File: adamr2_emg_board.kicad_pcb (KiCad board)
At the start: 2 copper layers, 50 x 50 mm, 7 parts, among them J1 Screw_Terminal_01x02, J2 Conn_01x02, J3 Screw_Terminal_01x02, K1 G6C-1114P-US

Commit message: Update
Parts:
- removed the REF** at (86.0, 94.0)
- removed the REF** at (126.0, 94.0)
- added REF**: MountingHole_3.2mm_M3, MountingHole:MountingHole_3.2mm_M3, F.Cu at (175.0, 69.8)
- added REF**: MountingHole_3.2mm_M3, MountingHole:MountingHole_3.2mm_M3, F.Cu at (124.5, 69.8)
- moved F1 52.8 mm to (171.0, 91.0)
- moved K1 51.1 mm to (154.0, 99.0), turned to 180 degrees
- moved J3 48.0 mm to (132.0, 99.0)
- moved J1 46.3 mm to (132.0, 84.0)
- moved J2 44.8 mm to (149.0, 85.0), turned to 90 degrees
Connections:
- K1 pad 3: Net-(F1-Pad2) -> Net-(J3-Pad2)
- K1 pad 4: Net-(J3-Pad2) -> Net-(F1-Pad2)
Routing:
- net VCC: track 60.0 -> 0.00 mm
- net Net-(F1-Pad2): track 28.1 -> 0.00 mm
- net Net-(J3-Pad2): track 14.8 -> 0.06 mm
- net Net-(J2-Pad1): track 9.98 -> 0.32 mm
- net GND: track 33.6 -> 28.0 mm
- removed copper zone on B.Cu, net GND
- removed copper zone on F.Cu, net GND
- removed copper zone on F.Cu, net Net-(F1-Pad2)
- removed copper zone on F.Cu, net Net-(J3-Pad2)
- removed copper zone on F.Cu, net VCC
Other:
- board size 50 x 50 mm -> 60 x 45 mm
- board text removed: "+24V"
- board text removed: "Emergency Switch"
- board text removed: "GND"
- board text removed: "INPUT"
- board text removed: "OUTPUT"
- board text removed: "Φ5.2x20mm Glass Tube Fuse"

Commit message: Update
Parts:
- removed J3: Screw_Terminal_01x02, adamr2_footprints:OSTYK21102030
- J1: value Screw_Terminal_01x02 -> Screw_Terminal_01x04; footprint adamr2_footprints:OSTYK21102030 -> adamr2_footprints:OSTYK21104030
- moved J1 8.81 mm to (133.3, 92.7)
- moved J2 4.82 mm to (153.7, 83.8)
- moved K1 2.21 mm to (156.2, 99.0)
- moved F1 1.72 mm to (172.7, 91.0)
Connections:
- J1 pad 2: VCC -> Net-(J1-Pad2)
- K1 pad 3: Net-(J3-Pad2) -> Net-(J1-Pad2)
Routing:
- net VCC: track 0.00 -> 48.4 mm
- net Net-(J1-Pad2): track 0.00 -> 26.3 mm
- net Net-(F1-Pad2): track 0.00 -> 16.2 mm
- net Net-(J2-Pad1): track 0.32 -> 13.3 mm
- net GND: track 28.0 -> 37.7 mm
- added copper zone on B.Cu, net GND
- added copper zone on F.Cu, net GND
- added copper zone on F.Cu, net Net-(F1-Pad2)
- added copper zone on F.Cu, net Net-(J1-Pad2)
- added copper zone on F.Cu, net VCC
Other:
- board text added: "5.2x20mm Glass Tube Fuse"
- board text added: "G6C-1114P-US DC24V"
- board text added: "GND"
- board text added: "INPUT"
- board text added: "OUTPUT"
- board text added: "VCC"
- board text added: "XH Conn"

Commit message: Update
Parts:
- added REF**: MountingHole_3.2mm_M3, MountingHole:MountingHole_3.2mm_M3, F.Cu at (118.0, 105.0)
- added REF**: MountingHole_3.2mm_M3, MountingHole:MountingHole_3.2mm_M3, F.Cu at (180.0, 105.0)
- moved REF** 12.0 mm to (118.0, 80.0)
- moved REF** 11.3 mm to (180.0, 80.0)
- moved F1 1.71 mm to (172.7, 92.7)
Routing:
- net VCC: track 48.4 -> 47.0 mm
- net Net-(F1-Pad2): track 16.2 -> 16.9 mm
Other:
- board size 60 x 45 mm -> 70 x 33 mm

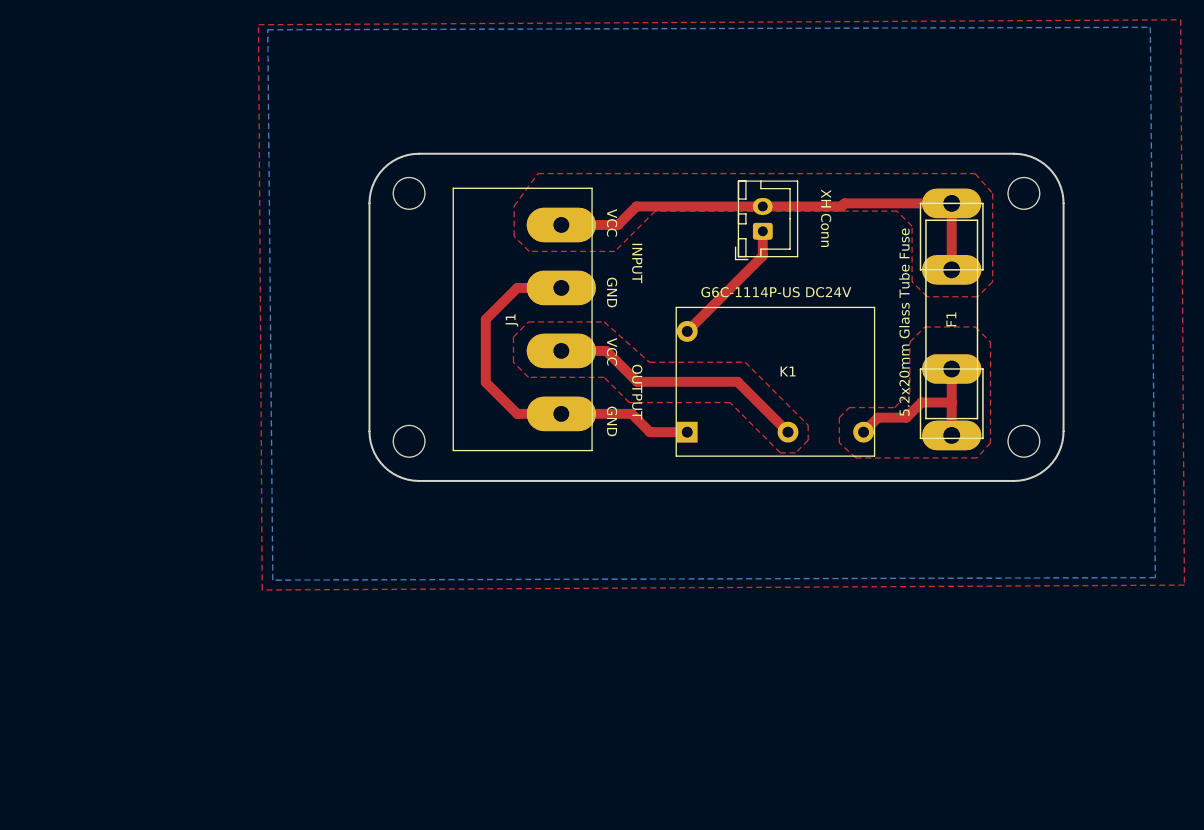
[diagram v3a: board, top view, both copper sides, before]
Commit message: Update: ヒューズホルダの種類を変更した
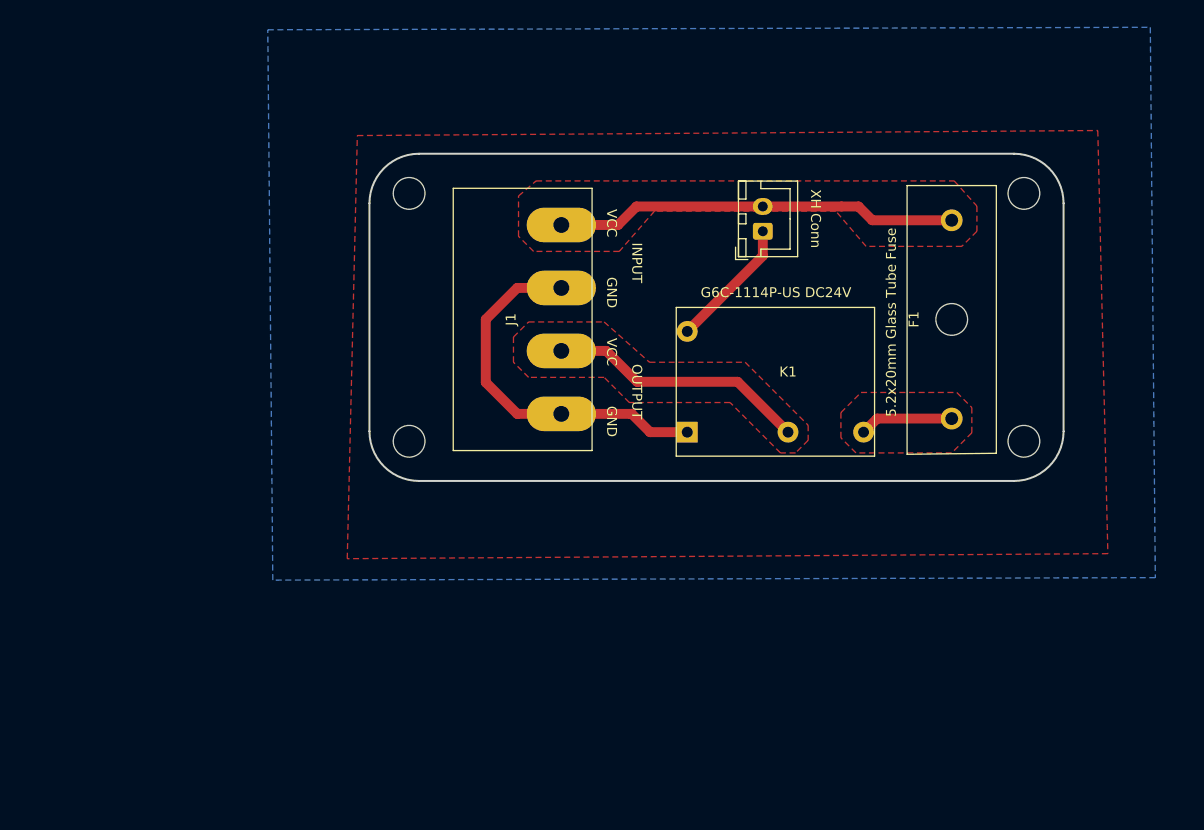
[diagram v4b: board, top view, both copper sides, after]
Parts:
- F1: footprint adamr2_footprints:FUC-03A -> adamr2_footprints:F-60-A
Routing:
- net Net-(F1-Pad2): track 16.9 -> 9.52 mm
- net VCC: track 47.0 -> 40.7 mm

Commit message: Update: 表面をVCC，裏面をGNDのベタにした
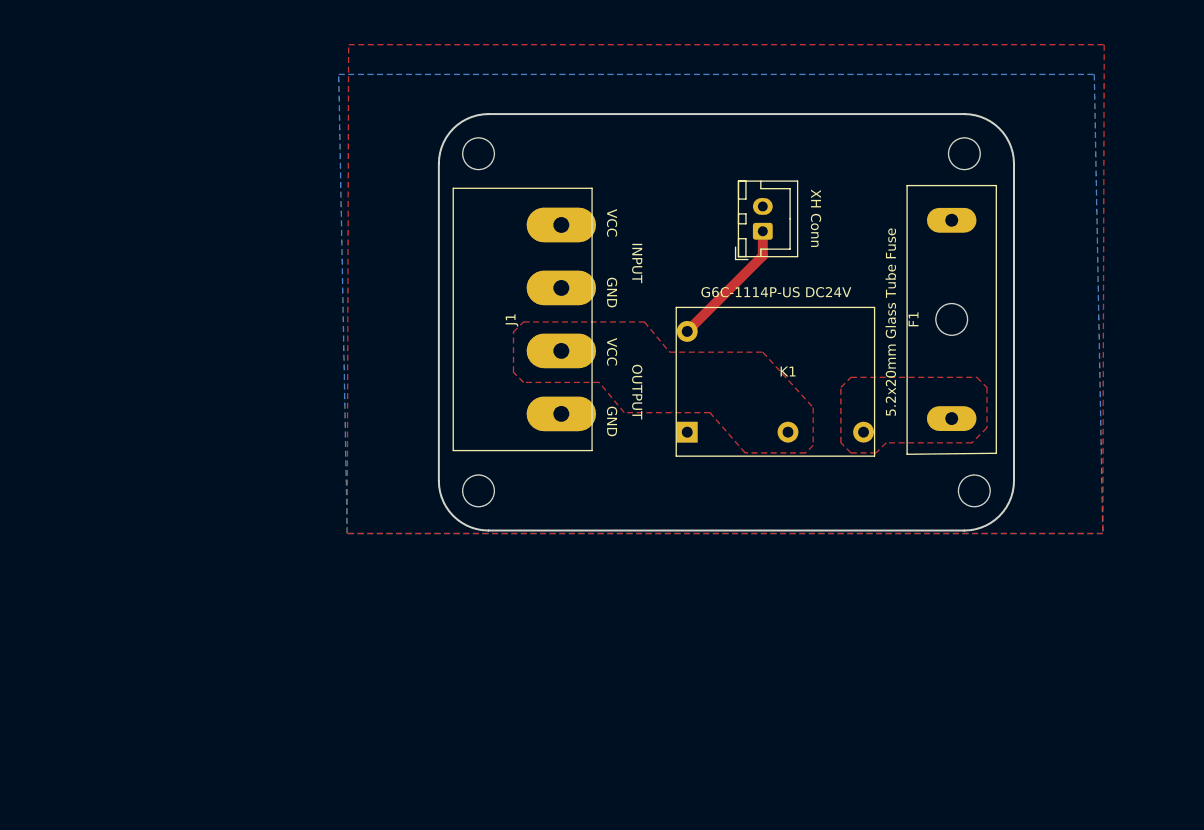
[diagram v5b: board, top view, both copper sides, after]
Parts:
- removed the REF** at (118.0, 80.0)
- removed the REF** at (118.0, 105.0)
- removed the REF** at (180.0, 105.0)
- removed the REF** at (180.0, 80.0)
- added REF**: MountingHole_3.2mm_M3, MountingHole:MountingHole_3.2mm_M3, F.Cu at (125.0, 76.0)
- added REF**: MountingHole_3.2mm_M3, MountingHole:MountingHole_3.2mm_M3, F.Cu at (125.0, 110.0)
- added REF**: MountingHole_3.2mm_M3, MountingHole:MountingHole_3.2mm_M3, F.Cu at (175.0, 110.0)
- added REF**: MountingHole_3.2mm_M3, MountingHole:MountingHole_3.2mm_M3, F.Cu at (174.0, 76.0)
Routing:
- net VCC: track 40.7 -> 0.00 mm
- net GND: track 37.7 -> 0.00 mm
- net Net-(J1-Pad2): track 26.3 -> 0.00 mm
- net Net-(F1-Pad2): track 9.52 -> 0.06 mm
- removed copper zone on F.Cu, net GND
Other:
- board size 70 x 33 mm -> 58 x 42 mm

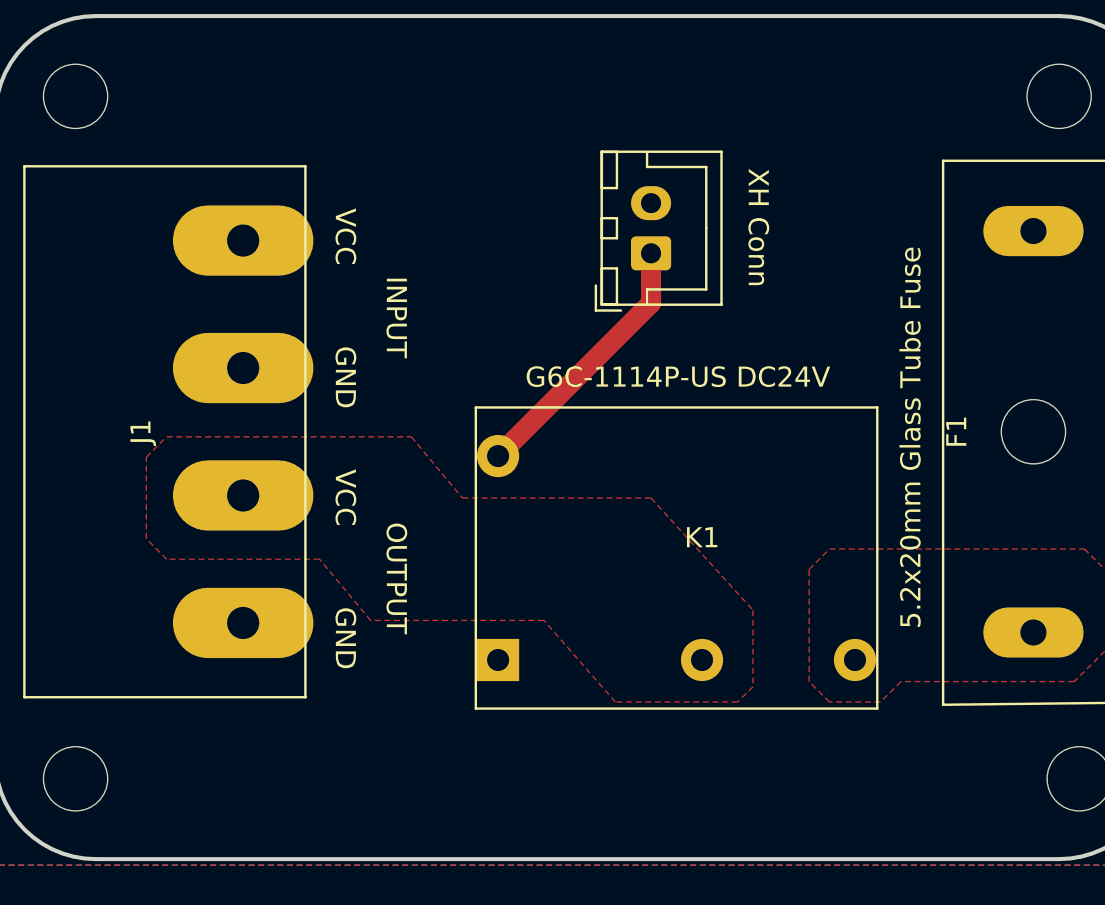
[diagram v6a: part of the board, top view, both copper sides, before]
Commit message: Update: シルクを少し調整，寸法線を追加
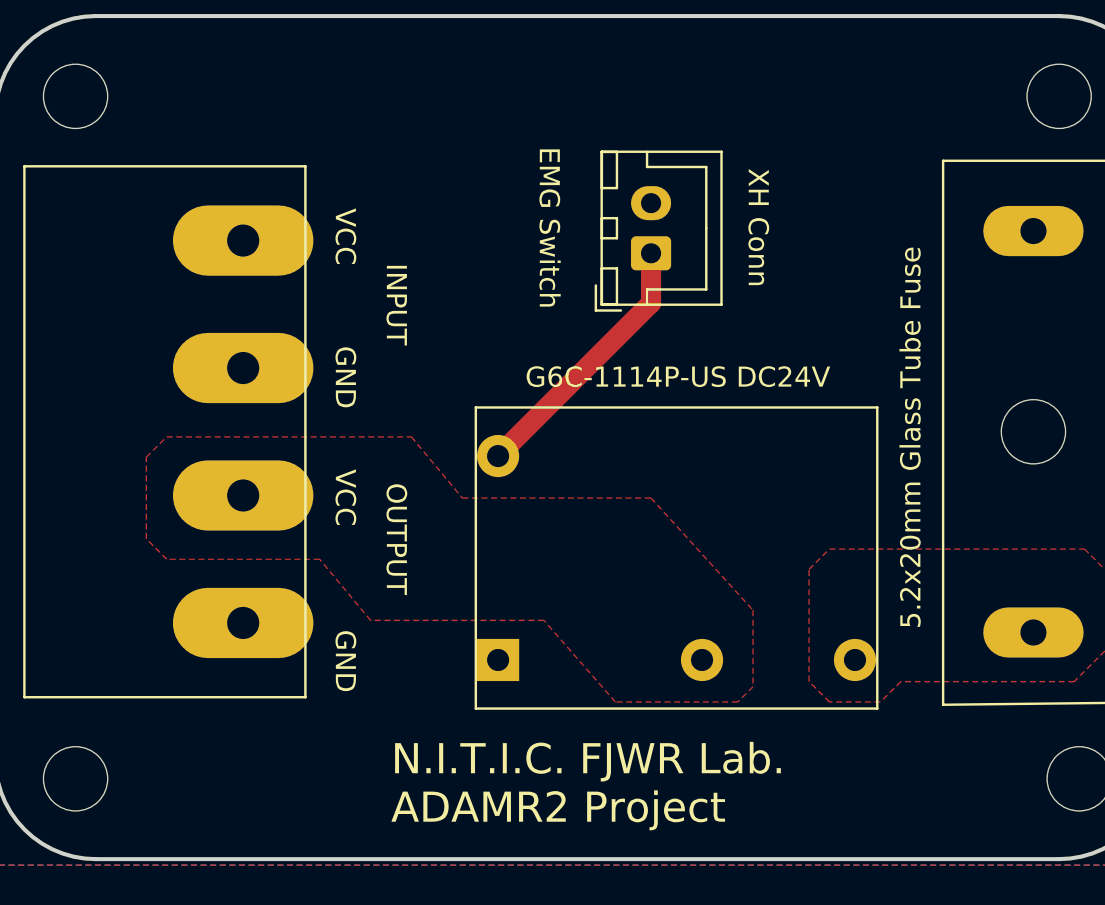
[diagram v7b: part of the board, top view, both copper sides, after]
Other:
- board text added: "EMG Switch"
- board text added: "N.I.T.I.C. FJWR Lab. ADAMR2 Project"
